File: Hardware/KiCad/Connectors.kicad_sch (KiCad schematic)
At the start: 55 parts

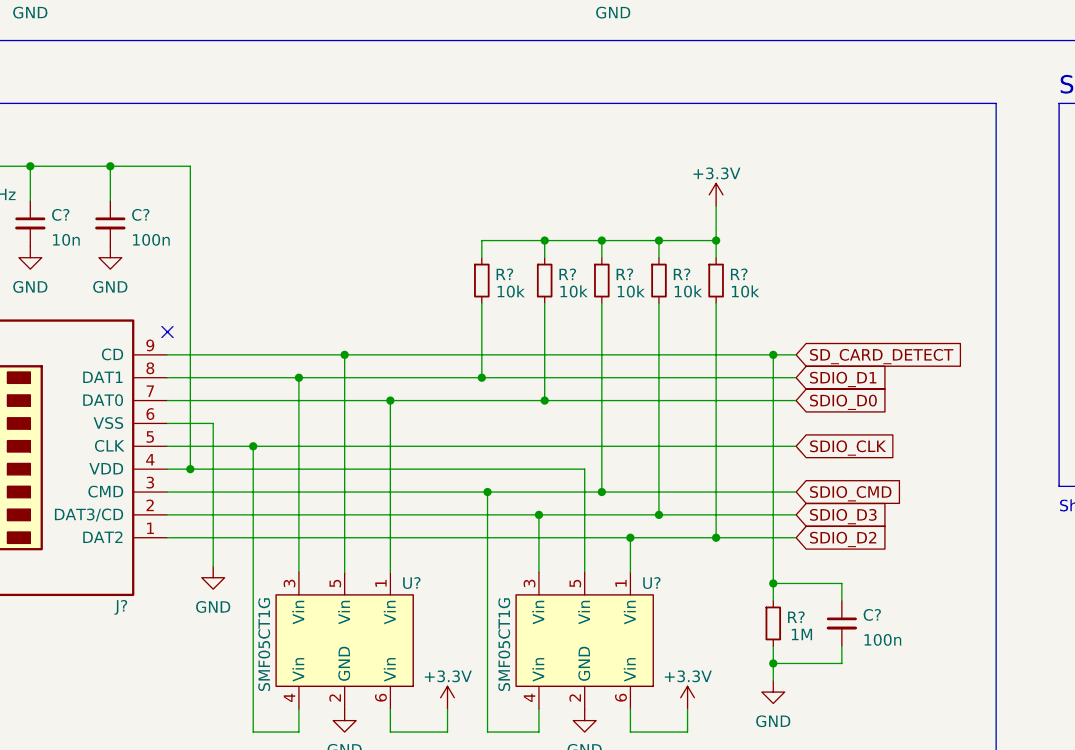
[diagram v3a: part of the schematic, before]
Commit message: Fixed pullup being a pulldown for SDIO CD, added SD test points
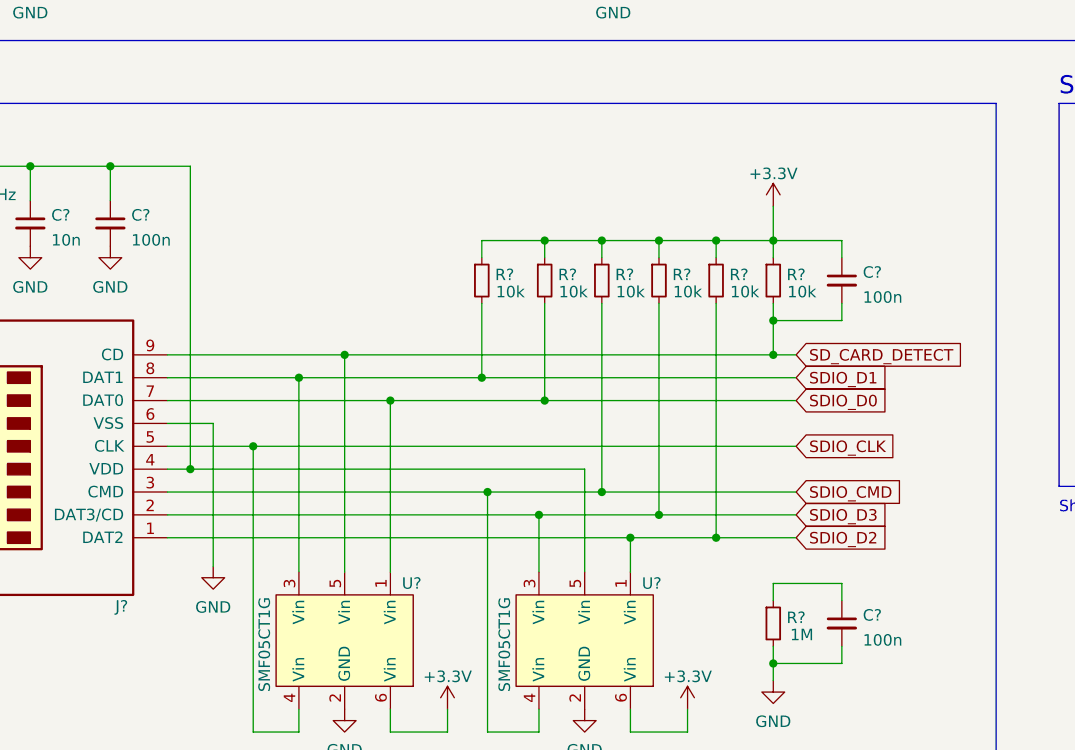
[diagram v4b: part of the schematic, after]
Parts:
- added C?: 100n, Capacitor_SMD:C_0402_1005Metric, symbol Device:C_Small
- added R?: 10k, Resistor_SMD:R_0402_1005Metric, symbol Device:R_Small
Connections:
- net +3V3: now also C?.1, R?.1
- net SD_CARD_DETECT: now also C?.2, R?.2; no longer C?.1, R?.1
- new net: C?.1, R?.1
- no-connect marks 8 -> 7
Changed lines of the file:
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@@
   (junction (at 93.345 52.07) (diameter 0) (color 0 0 0 0)
   )
+  (junction (at 132.08 93.345) (diameter 0) (color 0 0 0 0)
+  )
   (junction (at 79.375 108.585) (diameter 0) (color 0 0 0 0)
   )
@@
   (junction (at 193.675 144.78) (diameter 0) (color 0 0 0 0)
   )
+  (junction (at 132.08 102.235) (diameter 0) (color 0 0 0 0)
+  )
   (junction (at 39.37 34.925) (diameter 0) (color 0 0 0 0)
-  )
-  (junction (at 132.08 131.445) (diameter 0) (color 0 0 0 0)
   )
   (junction (at 269.24 35.56) (diameter 0) (color 0 0 0 0)
@@
   (no_connect (at 54.61 63.5))
   (no_connect (at 215.9 64.135))
-  (no_connect (at 64.77 103.505))
   (no_connect (at 149.225 42.545))
   (wire (pts (xy 103.505 40.005) (xy 114.3 40.005))
@@
     (stroke (width 0) (type default) (color 0 0 0 0))
   )
+  (wire (pts (xy 132.08 102.235) (xy 132.08 106.045))
+    (stroke (width 0) (type default) (color 0 0 0 0))
+  )
   (wire (pts (xy 184.15 88.9) (xy 177.8 88.9))
     (stroke (width 0) (type default) (color 0 0 0 0))
@@
     (stroke (width 0) (type default) (color 0 0 0 0))
   )
+  (wire (pts (xy 139.7 102.235) (xy 139.7 100.33))
+    (stroke (width 0) (type default) (color 0 0 0 0))
+  )
   (wire (pts (xy 168.91 93.345) (xy 168.91 96.52))
     (stroke (width 0) (type default) (color 0 0 0 0))
@@
     (stroke (width 0) (type default) (color 0 0 0 0))
   )
-  (wire (pts (xy 132.08 106.045) (xy 132.08 131.445))
-    (stroke (width 0) (type default) (color 0 0 0 0))
-  )
   (wire (pts (xy 196.215 142.24) (xy 196.215 147.32))
     (stroke (width 0) (type default) (color 0 0 0 0))
@@
     (stroke (width 0) (type default) (color 0 0 0 0))
   )
+  (wire (pts (xy 132.08 93.345) (xy 125.73 93.345))
+    (stroke (width 0) (type default) (color 0 0 0 0))
+  )
   (wire (pts (xy 196.215 157.48) (xy 198.755 157.48))
     (stroke (width 0) (type default) (color 0 0 0 0))
@@
     (stroke (width 0) (type default) (color 0 0 0 0))
   )
-  (wire (pts (xy 125.73 89.535) (xy 125.73 93.345))
+  (wire (pts (xy 132.08 89.535) (xy 132.08 93.345))
     (stroke (width 0) (type default) (color 0 0 0 0))
   )
@@
     (stroke (width 0) (type default) (color 0 0 0 0))
   )
+  (wire (pts (xy 132.08 100.33) (xy 132.08 102.235))
+    (stroke (width 0) (type default) (color 0 0 0 0))
+  )
   (wire (pts (xy 54.61 45.085) (xy 54.61 48.26))
     (stroke (width 0) (type default) (color 0 0 0 0))
@@
     (stroke (width 0) (type default) (color 0 0 0 0))
   )
+  (wire (pts (xy 139.7 95.25) (xy 139.7 93.345))
+    (stroke (width 0) (type default) (color 0 0 0 0))
+  )
   (wire (pts (xy 196.85 86.36) (xy 201.295 86.36))
     (stroke (width 0) (type default) (color 0 0 0 0))
@@
     (stroke (width 0) (type default) (color 0 0 0 0))
   )
+  (wire (pts (xy 132.08 102.235) (xy 139.7 102.235))
+    (stroke (width 0) (type default) (color 0 0 0 0))
+  )
   (polyline (pts (xy 182.88 19.685) (xy 182.88 71.12))
     (stroke (width 0) (type default) (color 0 0 0 0))
   )
+  (wire (pts (xy 132.08 95.25) (xy 132.08 93.345))
+    (stroke (width 0) (type default) (color 0 0 0 0))
+  )
   (wire (pts (xy 74.93 178.435) (xy 74.93 176.53))
     (stroke (width 0) (type default) (color 0 0 0 0))
@@
   )
   (wire (pts (xy 119.38 34.925) (xy 119.38 48.26))
+    (stroke (width 0) (type default) (color 0 0 0 0))
+  )
+  (wire (pts (xy 132.08 93.345) (xy 139.7 93.345))
     (stroke (width 0) (type default) (color 0 0 0 0))
   )
@@
     (pin "1")
   )
-  (symbol (lib_id "power:+3.3V") (at 125.73 89.535 0) (unit 1)
-    (in_bom yes) (on_board yes) (fields_autoplaced)
-    (property "Reference" "#PWR0142" (id 0) (at 125.73 93.345 0)
-      (effects (font (size 1.27 1.27)) hide)
-    )
-    (property "Value" "+3.3V" (id 1) (at 125.73 85.9305 0))
-    (property "Footprint" "" (id 2) (at 125.73 89.535 0)
-      (effects (font (size 1.27 1.27)) hide)
-    )
-    (property "Datasheet" "" (id 3) (at 125.73 89.535 0)
+  (symbol (lib_id "power:+3.3V") (at 132.08 89.535 0) (unit 1)
+    (in_bom yes) (on_board yes) (fields_autoplaced)
+    (property "Reference" "#PWR0142" (id 0) (at 132.08 93.345 0)
+      (effects (font (size 1.27 1.27)) hide)
+    )
+    (property "Value" "+3.3V" (id 1) (at 132.08 85.9305 0))
+    (property "Footprint" "" (id 2) (at 132.08 89.535 0)
+      (effects (font (size 1.27 1.27)) hide)
+    )
+    (property "Datasheet" "" (id 3) (at 132.08 89.535 0)
       (effects (font (size 1.27 1.27)) hide)
     )
@@
     )
     (pin "1")
+  )
+  (symbol (lib_id "Device:R_Small") (at 132.08 97.79 0) (unit 1)
+    (in_bom yes) (on_board yes)
+    (property "Reference" "R?" (id 0) (at 134.62 97.155 0))
+    (property "Value" "10k" (id 1) (at 135.255 99.06 0))
+    (property "Footprint" "Resistor_SMD:R_0402_1005Metric" (id 2) (at 132.08 97.79 0)
+      (effects (font (size 1.27 1.27)) hide)
+    )
+    (property "Datasheet" "~" (id 3) (at 132.08 97.79 0)
+      (effects (font (size 1.27 1.27)) hide)
+    )
+    (pin "1")
+    (pin "2")
   )
   (symbol (lib_id "flightController:SMF05CT1G") (at 232.41 56.515 180) (unit 1)
@@
     (pin "9")
   )
+  (symbol (lib_id "Device:C_Small") (at 139.7 97.79 0) (unit 1)
+    (in_bom yes) (on_board yes) (fields_autoplaced)
+    (property "Reference" "C?" (id 0) (at 142.0241 96.8878 0)
+      (effects (font (size 1.27 1.27)) (justify left))
+    )
+    (property "Value" "100n" (id 1) (at 142.0241 99.6629 0)
+      (effects (font (size 1.27 1.27)) (justify left))
+    )
+    (property "Footprint" "Capacitor_SMD:C_0402_1005Metric" (id 2) (at 139.7 97.79 0)
+      (effects (font (size 1.27 1.27)) hide)
+    )
+    (property "Datasheet" "~" (id 3) (at 139.7 97.79 0)
+      (effects (font (size 1.27 1.27)) hide)
+    )
+    (pin "1")
+    (pin "2")
+  )
   (symbol (lib_id "Device:R_Small") (at 135.89 34.925 90) (unit 1)
